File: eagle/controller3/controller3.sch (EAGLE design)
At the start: 37 parts, among them J1 FEMALE 2x3, J4 USB-MICROB

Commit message: controller3 update eagle files
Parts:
- removed C3: 100nF, SparkFun-Passives:CAPPTH
- removed R10, R11, R12: (no value), adafruit:R-US_R3225
- removed RES: (no value), SparkFun-FreqCtrl:RESONATORPTH
- removed U$1: ATMEGA32U4TQFP, SparkFun-Retired:ATMEGA32U4TQFP
- added C2: (no value), SparkFun-Capacitors:CAP1206
- added C4, C5: (no value), SparkFun-Passives:CAP1206
- added ICSP, ZERO: (no value), SparkFun-Connectors:M03X2FEMALE
- added Q1: (no value), adafruit:CRYSTALHC49U70
- added R4, R9, RB1, RB2, RB3, RDISP, RRST, RTEMP, RUSB1, RUSB2, RZERO, VD5, VD6: (no value), SparkFun-Passives:RESISTOR1206
- added T_CAM1, T_CAM2: (no value), SparkFun-DiscreteSemi:TRANSISTOR_NPN2N3904
- added U$3: ATMEGA32U4-AU, adafruit:ATMEGA32U4-AU
- J1: value FEMALE 2x3 -> (none); device SparkFun-Connectors:M03X2FEMALE -> SparkFun-Connectors:M02LOCK
- R1, R2, R3, R8: device adafruit:R-US_R3225 -> SparkFun-Passives:RESISTOR1206
- VD1, VD2, VD3, VD4: device adafruit:R-US_R3216 -> SparkFun-Passives:RESISTOR1206
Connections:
- removed net CAM_VCC: PWR_CAM.PWR
- removed net EXT_EN: U$1.PB6(ADC13)
- removed net N$7: J4.GND
- new net MISO: ICSP.1, U$3.PB3(PDO/MISO)
- new net MOSI: ICSP.4, U$3.PB2(PDI/MOSI)
- new net N$12: RZERO.1, T_ZERO.B
- new net N$13: RDISP.2, T_DISP.B
- new net N$14: J4.D+, RUSB1.2
- new net N$15: J4.D-, RUSB2.2
- new net N$16: J3.RIGHT, SHTR.2, T_CAM1.E
- new net N$17: J3.LEFT, SHTR.3, T_CAM2.E
- new net N$18: R2.2, T_CAM1.B
- new net N$19: R3.2, T_CAM2.B
- new net N$20: C2.2, U$3.UCAP
- new net N$21: MOSFET_CAM.G, R1.2, R4.1
- new net N$23: U$3.PD6(T1/ADC9/!OC4D)
- new net N$24: U$3.PD5(XCK/CTS)
- new net N$28: U$3.PB7(OC0A/OC1C/RTS)
- new net SCK: ICSP.3, U$3.PB1(SCK)
- new net VD_DIRECT: U$3.PB4(ADC11), VD5.1, VD6.2
- net BATT_VCC: now also PWR_CAM.PWR, VD5.2
- net BTN1: now also RB1.2, U$3.PF0(ADC0); no longer R11.2, U$1.PF5(ADC5)
- net BTN2: now also RB2.2, U$3.PF1(ADC1); no longer R8.2, U$1.PF4(ADC4)
- net BTN3: now also RB3.2, U$3.PF4(ADC4/TCK); no longer R10.2, U$1.PF1(ADC1)
- net CAM1: now also R2.1, U$3.PC7(ICP3/CLK0/OC4A); no longer J3.LEFT, SHTR.3, U$1.PC7
- net CAM2: now also R3.1, U$3.PC6(OC3A/!OC4A); no longer J3.RIGHT, SHTR.2, U$1.PD6(ADC9)
- net CAM_EN: now also R4.2, U$3.PD7(OC4D/ADC10/T0); no longer MOSFET_CAM.G, U$1.PB7
- net CELL1: now also U$3.PB5(OC1A/ADC12/!OC4B), VD3.2; no longer U$1.PF6(ADC6), VD1.2, VD2.1
- net CELL2: now also U$3.PB6(OC1B/OC4B/ADC13), VD1.2, VD2.1; no longer U$1.PF7(ADC7), VD3.2
- net DISP_EN: now also RDISP.1, U$3.PF6(ADC6/TDO); no longer T_DISP.B, U$1.PC6
- net DISP_RST: now also U$3.PF7(ADC7(TDI); no longer U$1.PB4(ADC11)
- net GND: now also BTN_DW.1, BTN_UP.1, BTN_X.1, C2.1, C4.1, C5.1, ICSP.6, J4.GND, R1.1, T_CAM1.C, T_CAM2.C, U$3.GND, U$3.GND1, U$3.GND2, U$3.GND3, U$3.PE2(!HWB), U$3.UGND, VD6.1, ZERO.4; no longer BTN_DW.2, BTN_UP.2, BTN_X.2, C3.1, J1.4, RES.2, U$1.GND@15, U$1.GND@23, U$1.GND@35, U$1.GND@43, U$1.UGND
- net N$1: now also RRST.1, U$3./RESET; no longer R12.2, U$1.!RESET
- net N$10: now also ZERO.2; no longer J1.2
- net N$11: now also J1.1, U$3.VBUS; no longer U$1.VBUS
- net N$4: now also RUSB1.1, U$3.D-; no longer J4.D-, U$1.D-
- net N$5: now also RUSB2.1, U$3.D+; no longer J4.D+, U$1.D+
- net N$8: now also C4.2, Q1.2, U$3.XTAL1; no longer RES.3
- net N$9: now also C5.2, Q1.1, U$3.XTAL2; no longer RES.1
- net RST: now also ICSP.5, ZERO.6; no longer J1.6
- net RX: now also U$3.PD2(INT2/RXD1), ZERO.3; no longer J1.3, U$1.PD2(RX)
- net SCL: now also R8.1, U$3.PD0(INT0/OC0B/SCL); no longer R3.2, U$1.PD0(SCL)
- net SDA: now also R9.2, U$3.PD1(INT1/SDA); no longer R1.1, U$1.PD1(SDA)
- net TEMP: now also RTEMP.1, U$3.PF5(ADC5/TMS); no longer R2.2, U$1.PB5(ADC12)
- net TX: now also U$3.PD3(INT3/TXD1), ZERO.5; no longer J1.5, U$1.PD3(TX)
- net VCC: now also ICSP.2, J1.2, R8.2, R9.1, RB1.1, RB2.1, RB3.1, RRST.2, RTEMP.2, U$3.AVCC, U$3.AVCC1, U$3.UVCC, U$3.VCC, U$3.VCC1, ZERO.1; no longer C3.2, J1.1, R1.2, R10.1, R11.1, R12.1, R2.1, R3.1, R8.1, U$1.AREF, U$1.AVCC@24, U$1.AVCC@44, U$1.VCC@14, U$1.VCC@34
- net ZERO_EN: now also RZERO.2, U$3.PD4(ICP1/ADC8); no longer T_ZERO.B, U$1.PD7(ADC10)
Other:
- moved on the sheet: C1, CONV_X_VCC, J3, J4, PWR_BATT, PWR_CAM, R1, R2, R3, R8, SHTR

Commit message: controller3: eagle files update
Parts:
- removed U$2: V_REG_LD1117VXX, SparkFun-PowerIC:V_REG_LD1117VXX
- added C3: 10uF, SparkFun-Passives:CAP1206
- C1: device SparkFun-Passives:CAPPTH -> SparkFun-Passives:CAP1206
- C2: value (none) -> 1uF
- Q1: device adafruit:CRYSTALHC49U70 -> adafruit:CRYSTALCTS406
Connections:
- new net N$22: C3.1, J4.VBUS
- net N$11: now also C3.2; no longer J4.VBUS
- net VCC: now also DISP.6; no longer DISP.5

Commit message: controller 2.4 / 3.0 changes
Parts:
- removed MOSFET_CAM: MOSFET-NCHANNELFQP30N06L, SparkFun-DiscreteSemi:MOSFET-NCHANNELFQP30N06L
- removed RDISP, RZERO: (no value), SparkFun-Passives:RESISTOR1206
- removed T_DISP, T_ZERO: (no value), SparkFun-DiscreteSemi:TRANSISTOR_NPN2N3904
- added Q2: MOSFET-PCHANNELFQP27P06, SparkFun-DiscreteSemi:MOSFET-PCHANNELFQP27P06
- added T_ZERO1: (no value), SparkFun-DiscreteSemi:TRANSISTOR_NPN2N3904
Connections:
- removed net N$12: RZERO.1, T_ZERO.B
- removed net N$13: RDISP.2, T_DISP.B
- removed net N$6: DISP.4, T_DISP.C
- new net N$7: R4.2, T_ZERO1.B
- net BATT_VCC: now also Q2.D, R1.1; no longer PWR_CAM.PWR
- net CAM1: now also U$3.PC6(OC3A/!OC4A); no longer U$3.PC7(ICP3/CLK0/OC4A)
- net CAM2: now also U$3.PC7(ICP3/CLK0/OC4A); no longer U$3.PC6(OC3A/!OC4A)
- net CAM_EN: now also R4.1; no longer R4.2
- net CAM_OUT: now also PWR_CAM.PWR, Q2.S; no longer MOSFET_CAM.D, PWR_CAM.GND
- net DISP_EN: no longer RDISP.1
- net GND: now also DISP.4, T_ZERO1.E; no longer R1.1, T_DISP.E, T_ZERO.E
- net GNDA: now also PWR_CAM.GND; no longer MOSFET_CAM.S
- net N$10: no longer T_ZERO.C
- net N$16: now also SHTR.3; no longer SHTR.2
- net N$17: now also SHTR.2; no longer SHTR.3
- net N$21: now also Q2.G, T_ZERO1.C; no longer MOSFET_CAM.G, R4.1
- net ZERO_EN: no longer RZERO.2
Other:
- note added: "Beim P-Channel Mosfet unbedingt nochmal die Eingänge checken"
- note removed: "TODO: Pull-Resistor for Mosfet. Maybe even an Transistor on the gate"
- moved on the sheet: R1, R4

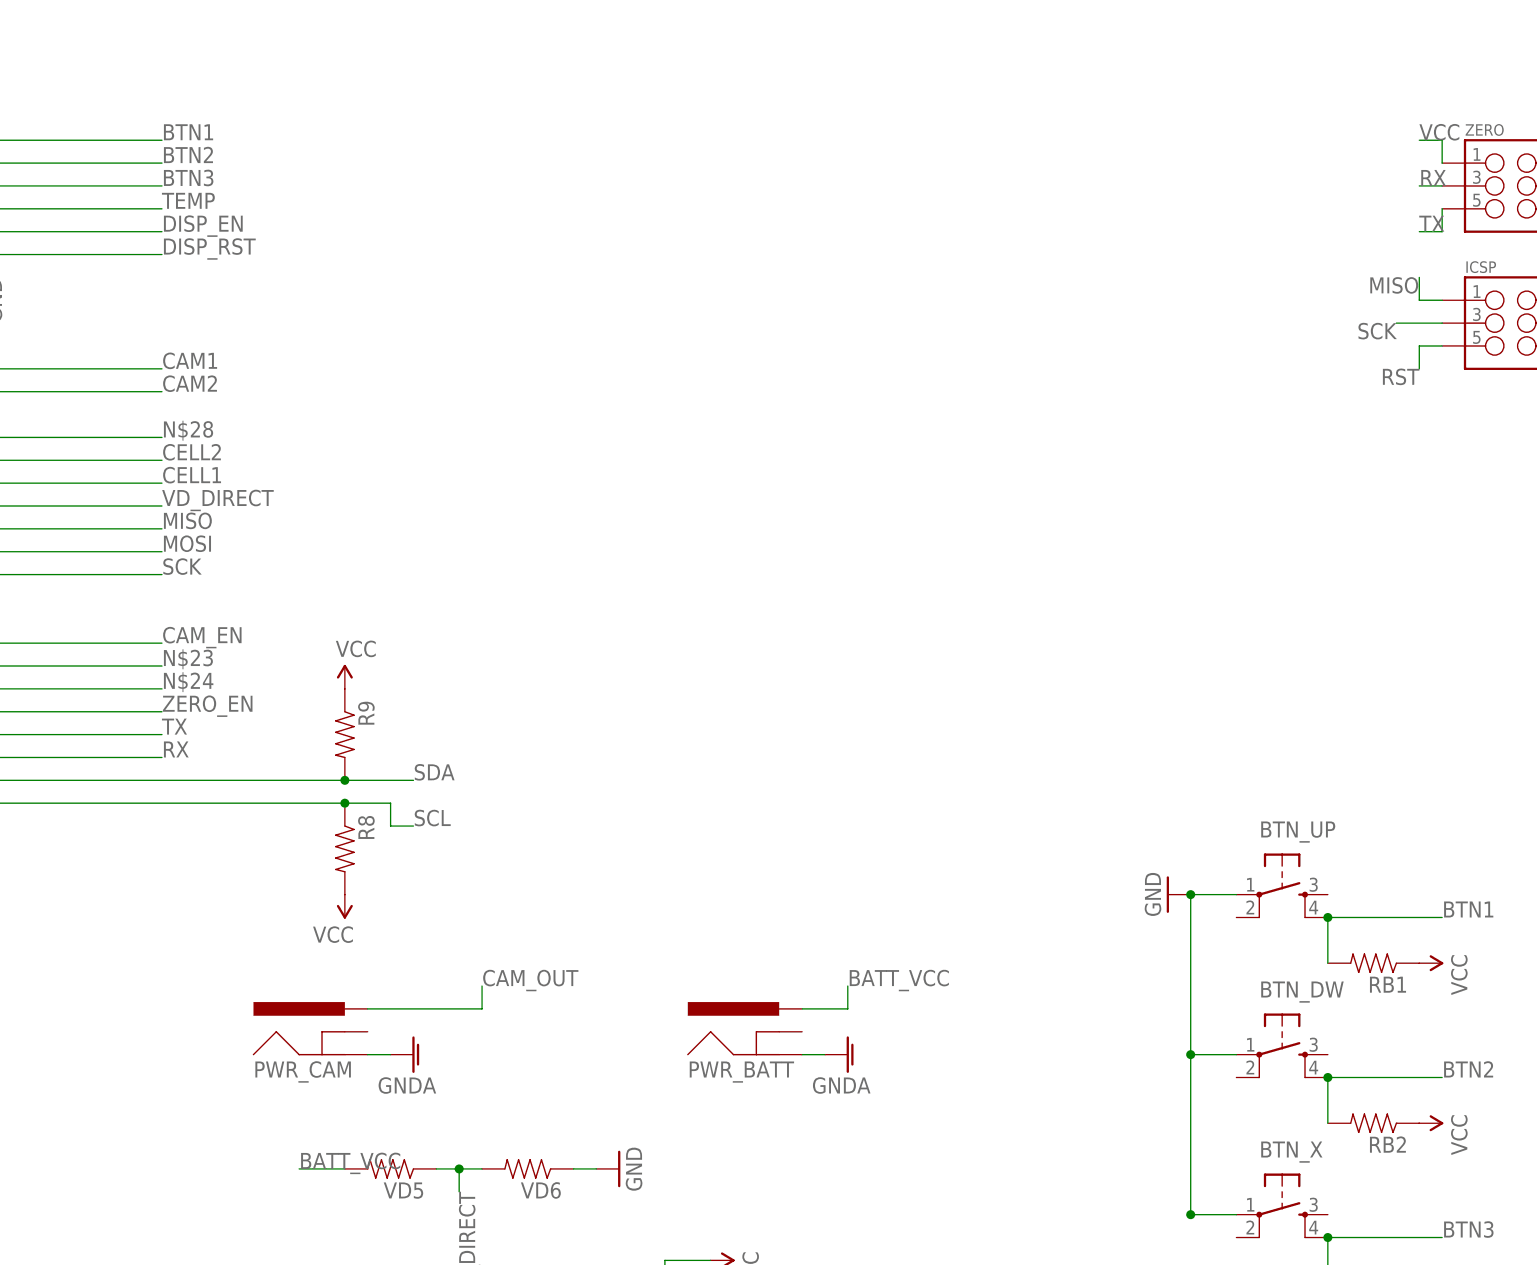
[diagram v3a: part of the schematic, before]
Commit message: controller3: changed board layout for milling
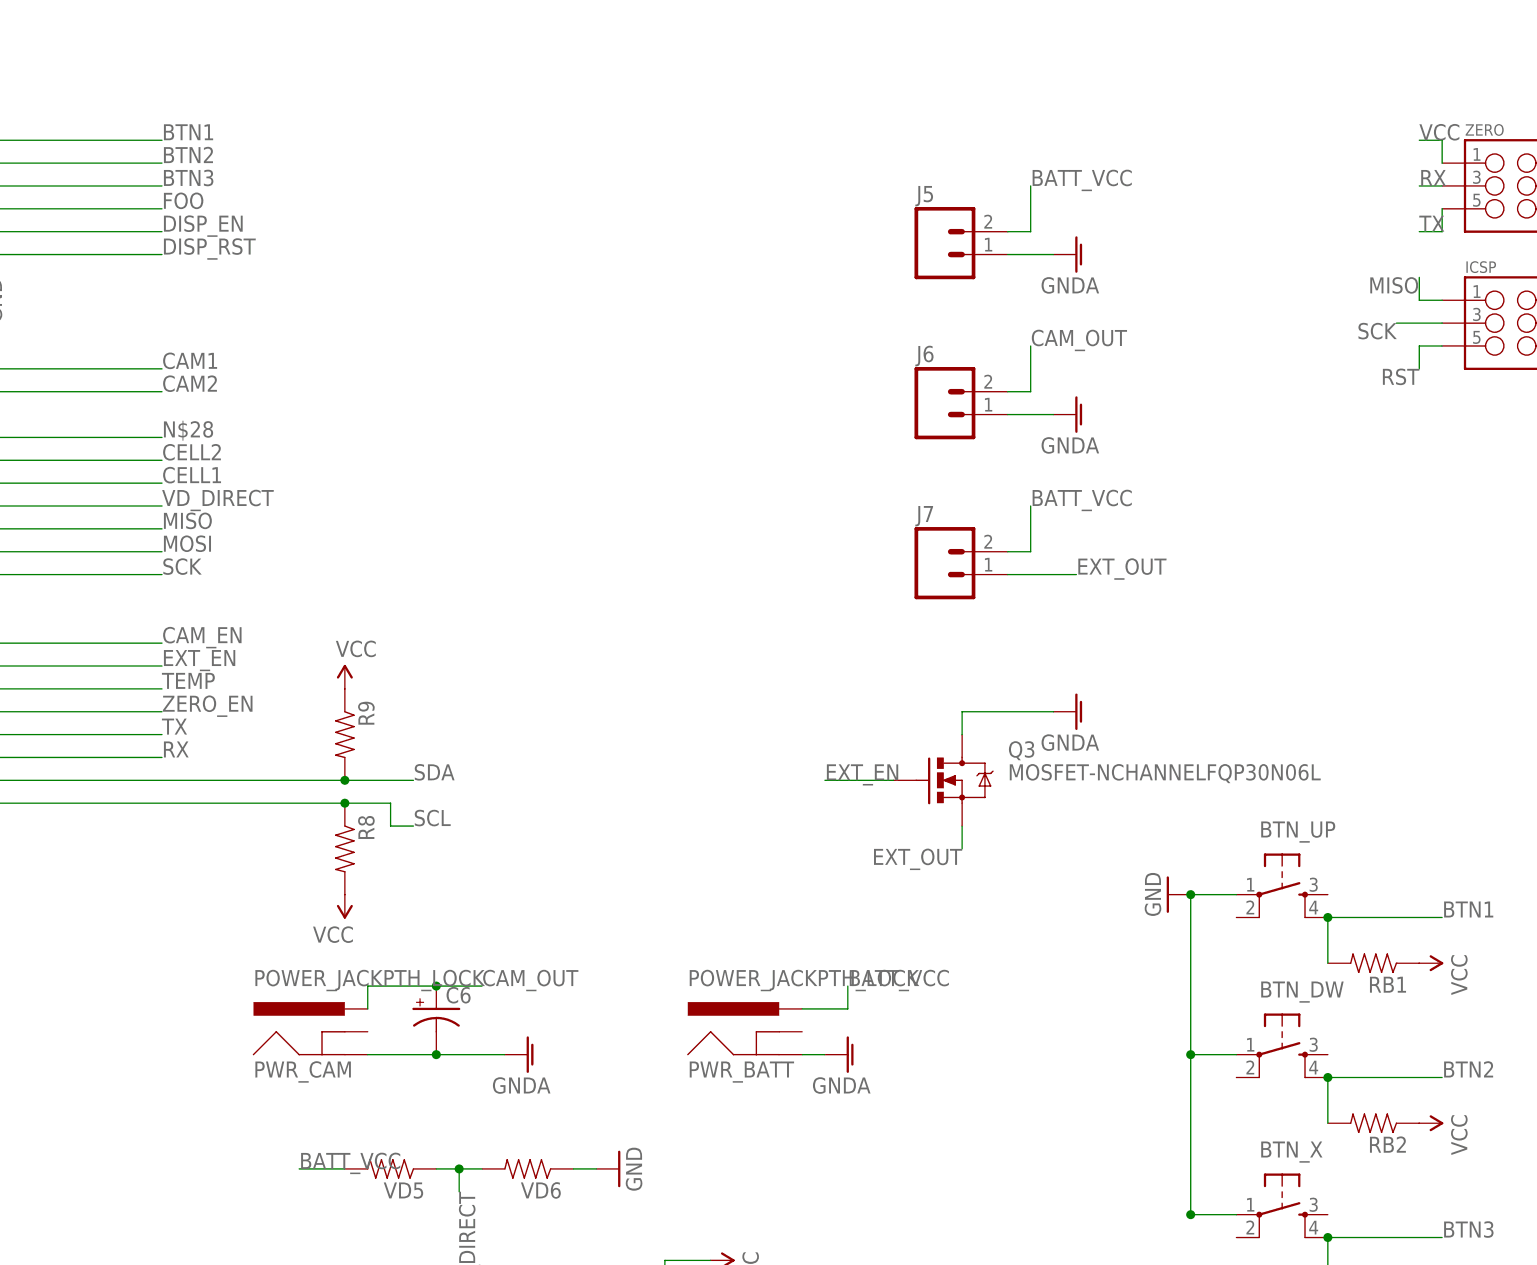
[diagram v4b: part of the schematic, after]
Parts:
- added C6: (no value), SparkFun-Capacitors:CAP_POLPTH3
- added J5, J6, J7: (no value), SparkFun-Connectors:M025MM
- added Q3: MOSFET-NCHANNELFQP30N06L, SparkFun-DiscreteSemi:MOSFET-NCHANNELFQP30N06L
- C2: device SparkFun-Capacitors:CAP1206 -> SparkFun-Capacitors:CAPPTH1
- C3: device SparkFun-Passives:CAP1206 -> SparkFun-Passives:CAPPTH1
- PWR_BATT, PWR_CAM: value POWER_JACKPTH_BREAD -> POWER_JACKPTH_LOCK; device SparkFun-Connectors:POWER_JACKPTH_BREAD -> SparkFun-Connectors:POWER_JACKPTH_LOCK
- Q1: device adafruit:CRYSTALCTS406 -> adafruit:CRYSTALHC49S
- R3, RUSB1, RUSB2: device SparkFun-Passives:RESISTOR1206 -> SparkFun-Passives:RESISTORAXIAL-0.3
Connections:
- removed net N$23: U$3.PD6(T1/ADC9/!OC4D)
- removed net N$24: U$3.PD5(XCK/CTS)
- new net EXT_EN: Q3.G, U$3.PD6(T1/ADC9/!OC4D)
- new net EXT_OUT: J7.1, Q3.S
- new net FOO: U$3.PF5(ADC5/TMS)
- net BATT_VCC: now also J5.2, J7.2
- net CAM_OUT: now also C6.+, J6.2
- net GNDA: now also C6.-, J5.1, J6.1, Q3.D
- net TEMP: now also U$3.PD5(XCK/CTS); no longer U$3.PF5(ADC5/TMS)

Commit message: bulk commit (eagle files, old changes)
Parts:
- C2: device SparkFun-Capacitors:CAPPTH1 -> SparkFun-Capacitors:CAP1206
- C3: device SparkFun-Passives:CAPPTH1 -> SparkFun-Passives:CAP1206
- R3, RUSB1, RUSB2: device SparkFun-Passives:RESISTORAXIAL-0.3 -> SparkFun-Passives:RESISTOR1206
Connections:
- removed net N$14: J4.D+, RUSB1.2
- removed net N$15: J4.D-, RUSB2.2
- removed net N$22: C3.1, J4.VBUS
- new net N$12: J4.D-, RUSB1.2
- new net N$13: J4.D+, RUSB2.2
- new net N$6: C3.1, J4.VBUS, U$3.UVCC
- net VCC: no longer U$3.UVCC
